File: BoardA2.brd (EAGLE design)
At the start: 44 x 93 mm, 17 parts, among them J1 FEMALE 2x3, T1 2N2222

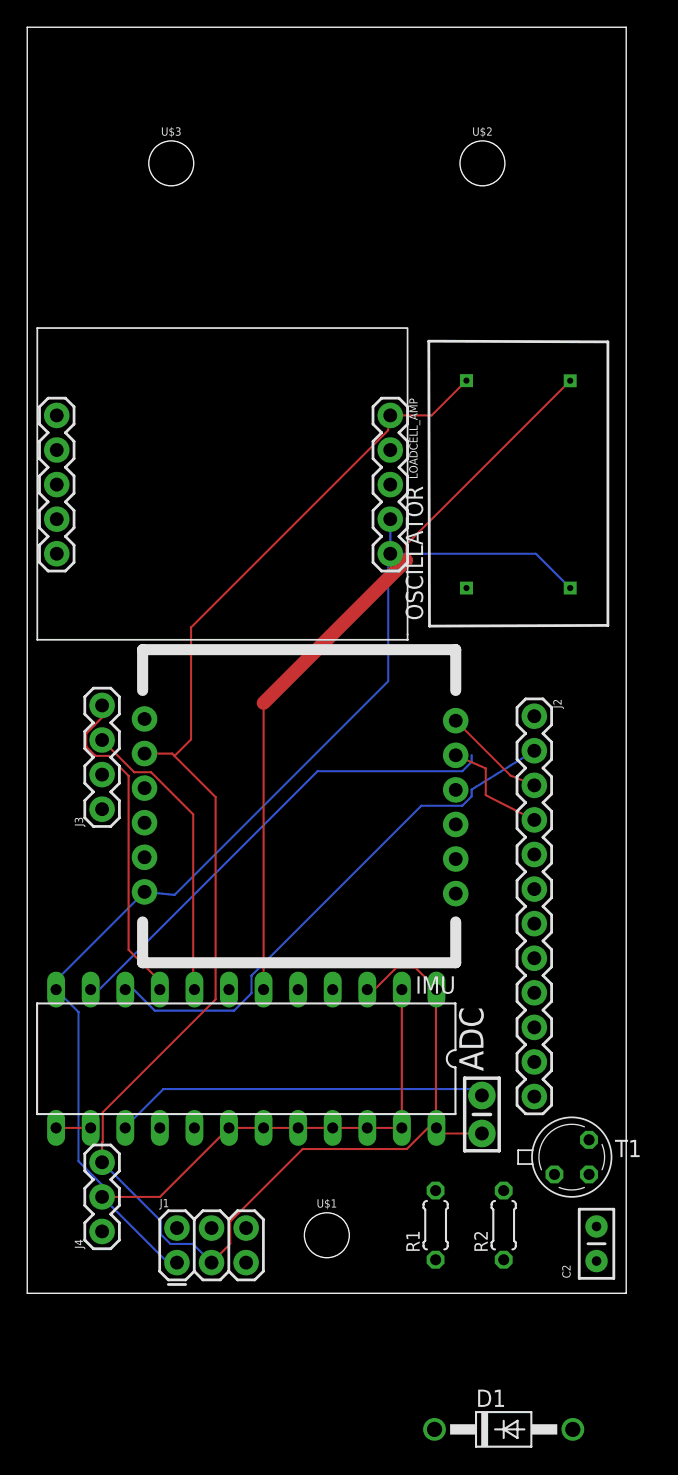
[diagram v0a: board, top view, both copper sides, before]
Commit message: routed middle board
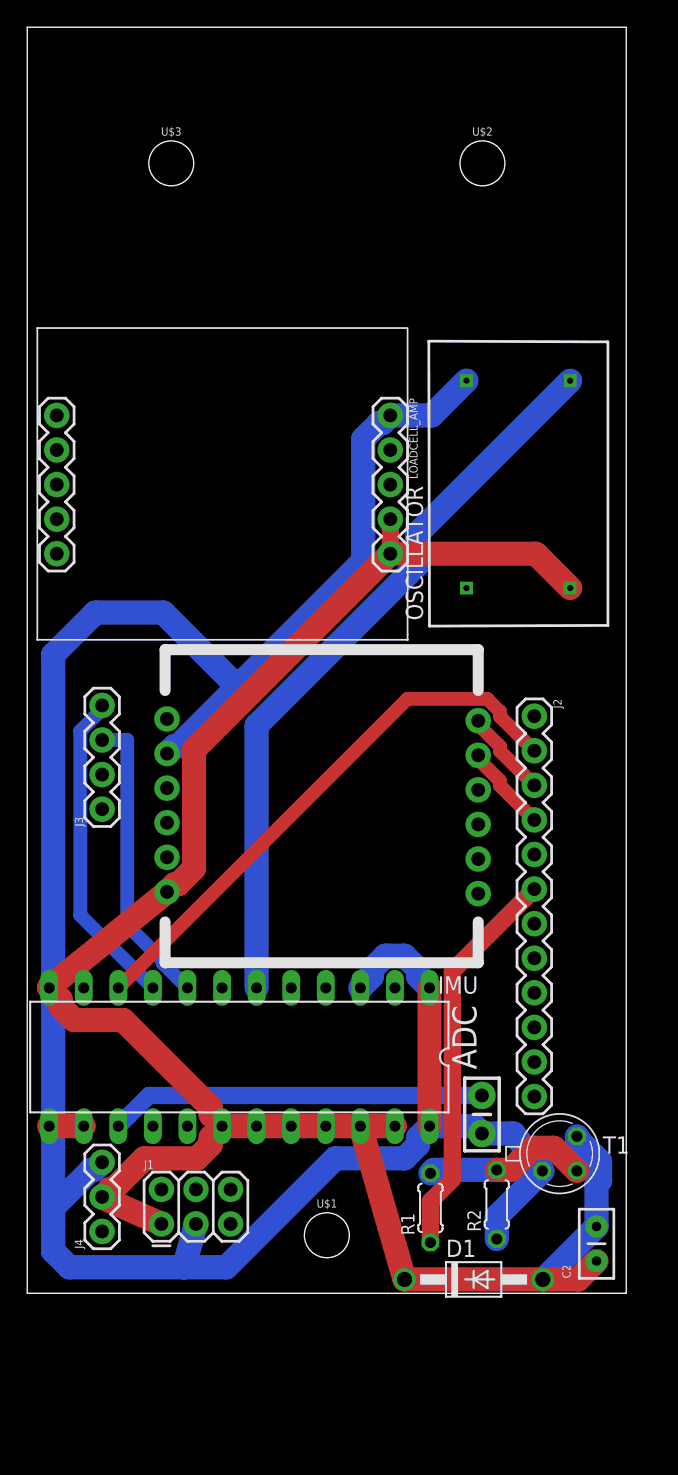
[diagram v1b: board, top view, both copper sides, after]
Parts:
- moved D1 11.2 mm to (32.8, 1.02)
- moved J1 3.06 mm to (9.86, 5.09)
- moved IMU 1.65 mm to (33.1, 24.3)
- moved R2 1.61 mm to (34.5, 6.52)
- moved R1 1.33 mm to (29.6, 6.27)
- moved T1 0.92 mm to (39.1, 10.3)
- moved ADC 0.52 mm to (15.6, 17.4)
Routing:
- net GND: track 128.5 -> 173.9 mm
- net DIN: track 35.4 -> 0.00 mm
- net TEENSY6: track 0.00 -> 29.1 mm
- net 5V: track 118.9 -> 132.1 mm
- net N$6: track 0.00 -> 13.0 mm
- net N$8: track 0.00 -> 12.2 mm
- net TXD: track 8.38 -> 6.46 mm
- net DOUT: track 39.3 -> 41.1 mm
- net RXD: track 7.58 -> 6.46 mm
- net RFS: track 24.2 -> 23.6 mm

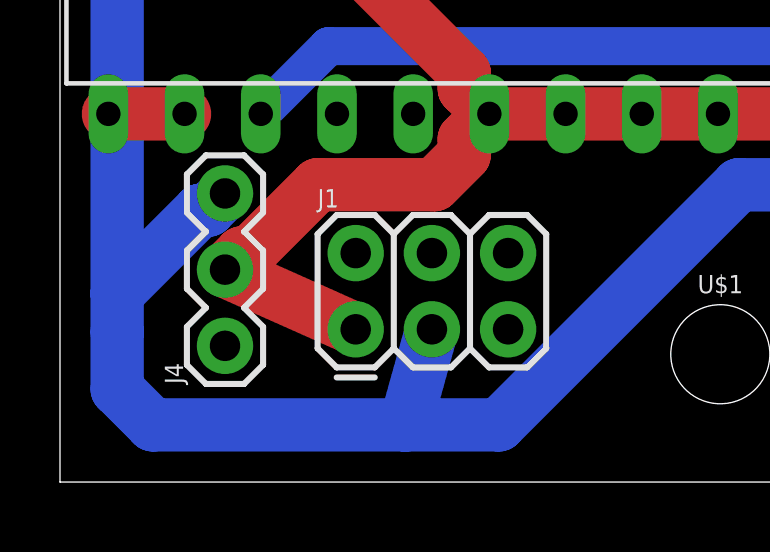
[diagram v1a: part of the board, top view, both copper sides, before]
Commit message: made wire and vias thicker
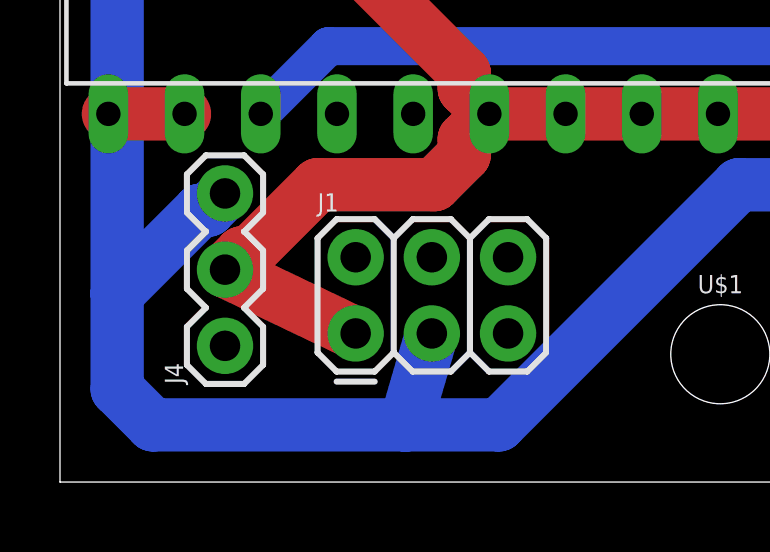
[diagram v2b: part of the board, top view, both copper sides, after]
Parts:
- moved J1 0.14 mm to (9.86, 4.95)
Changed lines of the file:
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@@
 </element>
 <element name="ADC" library="ic-package" library_urn="urn:adsk.eagle:library:239" package="DIL24-4" value="AD7890-10" x="15.582" y="17.353" rot="R180"/>
-<element name="J1" library="SparkFun-Connectors" package="2X3" value="FEMALE 2x3" x="9.857" y="5.091">
-<attribute name="PROD_ID" value="CONN-11566" x="9.857" y="5.091" size="1.778" layer="27" display="off"/>
+<element name="J1" library="SparkFun-Connectors" package="2X3" value="FEMALE 2x3" x="9.8552" y="4.953">
+<attribute name="PROD_ID" value="CONN-11566" x="9.8552" y="4.953" size="1.778" layer="27" display="off"/>
 </element>
 <element name="OSCILLATOR" library="Smartcrutches" package="ECS-100X" value="CLOCK-ECS-100X" x="36.077" y="59.422" rot="R90"/>
@@
 <wire x1="8.59264375" y1="9.9108" x2="6.32064375" y2="7.6388" width="1.778" layer="1"/>
 <wire x1="5.5" y1="7.035" x2="5.5" y2="7.08" width="1.778" layer="1"/>
-<wire x1="9.857" y1="5.091" x2="5.5" y2="7.035" width="1.778" layer="1"/>
+<wire x1="9.8552" y1="4.953" x2="5.5" y2="7.035" width="1.778" layer="1"/>
 <wire x1="3.4470875" y1="20.0708" x2="2.4502" y2="21.0676875" width="1.778" layer="1"/>
 <wire x1="2.4502" y1="21.0676875" x2="2.4502" y2="21.5948" width="1.778" layer="1"/>
@@
 <contactref element="T1" pad="1"/>
 <contactref element="R2" pad="1"/>
-<wire x1="12.397" y1="5.091" x2="11.508" y2="1.905" width="1.778" layer="16"/>
+<wire x1="12.3952" y1="4.953" x2="11.508" y2="1.905" width="1.778" layer="16"/>
 <wire x1="11.508" y1="1.905" x2="3.095" y2="1.905" width="1.778" layer="16"/>
 <wire x1="3.095" y1="1.905" x2="1.905" y2="3.095" width="1.778" layer="16"/>
 <wire x1="4.67935625" y1="9.0612" x2="4.9412" y2="9.0612" width="1.778" layer="16"/>
 <wire x1="4.9412" y1="9.0612" x2="5.5" y2="9.62" width="1.778" layer="16"/>
-<wire x1="1.905" y1="3.095" x2="1.905" y2="5" width="1.778" layer="16"/>
-<wire x1="1.905" y1="5" x2="1.905" y2="6.28684375" width="1.778" layer="16"/>
+<wire x1="1.905" y1="3.095" x2="1.905" y2="6.28684375" width="1.778" layer="16"/>
 <wire x1="1.905" y1="6.28684375" x2="4.67935625" y2="9.0612" width="1.778" layer="16"/>
 <wire x1="27.7169125" y1="9.9108" x2="28.7138" y2="10.9076875" width="1.778" layer="16"/>

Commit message: Teensy Pin Update 1
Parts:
- renumbered J2 to TEENSY1-12
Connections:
- removed net TEENSY9: TEENSY1-12.9
- new net IMU-RX: IMU.7, TEENSY1-12.10
- new net IMU-TX: IMU.8, TEENSY1-12.9
- net DOUT: no longer TEENSY1-12.2
- net RXD: no longer IMU.7
- net TXD: no longer IMU.8
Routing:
- net DOUT: track 41.1 -> 37.6 mm
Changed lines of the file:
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@@
 <element name="IMU" library="Smartcrutches" package="IMU" value="TSS-EM/3Space" x="33.128" y="24.278" rot="R180"/>
 <element name="LOADCELL_AMP" library="Smartcrutches" package="LOADCELLAMP2" value="HX711" x="15.24" y="59.403" rot="R180"/>
-<element name="J2" library="SparkFun-Connectors" package="1X12" value="" x="37.25" y="42.39" rot="R270"/>
+<element name="TEENSY1-12" library="SparkFun-Connectors" package="1X12" value="" x="37.25" y="42.39" rot="R270"/>
 <element name="J3" library="SparkFun-Connectors" package="1X04" value="" x="5.5" y="35.56" rot="R90">
 <attribute name="PROD_ID" value="CONN-09696" x="5.5" y="35.56" size="1.778" layer="27" rot="R90" display="off"/>
@@
 <signal name="DOUT">
 <contactref element="ADC" pad="10"/>
-<contactref element="J2" pad="2"/>
 <wire x1="33.790825" y1="43.6582" x2="34.7282" y2="42.720825" width="1.016" layer="1"/>
 <wire x1="6.692" y1="22.433" x2="6.70370625" y2="22.433" width="1.016" layer="1"/>
 <wire x1="34.7282" y1="42.720825" x2="34.7282" y2="42.3718" width="1.016" layer="1"/>
-<wire x1="34.7282" y1="42.3718" x2="37.25" y2="39.85" width="1.016" layer="1"/>
 <wire x1="6.70370625" y1="22.433" x2="27.92890625" y2="43.6582" width="1.016" layer="1"/>
 <wire x1="27.92890625" y1="43.6582" x2="33.790825" y2="43.6582" width="1.016" layer="1"/>
@@
 </signal>
 <signal name="TXD">
-<contactref element="IMU" pad="8"/>
-<contactref element="J2" pad="4"/>
+<contactref element="TEENSY1-12" pad="4"/>
 <wire x1="34.7282" y1="37.640825" x2="34.7282" y2="37.2918" width="1.016" layer="1"/>
 <wire x1="34.7282" y1="37.2918" x2="37.25" y2="34.77" width="1.016" layer="1"/>
-<wire x1="33.128" y1="39.518" x2="33.128" y2="39.241025" width="1.016" layer="1"/>
 <wire x1="33.128" y1="39.241025" x2="34.7282" y2="37.640825" width="1.016" layer="1"/>
 </signal>
 <signal name="RXD">
-<contactref element="IMU" pad="7"/>
-<contactref element="J2" pad="3"/>
+<contactref element="TEENSY1-12" pad="3"/>
 <wire x1="34.7282" y1="40.180825" x2="34.7282" y2="39.8318" width="1.016" layer="1"/>
 <wire x1="34.7282" y1="39.8318" x2="37.25" y2="37.31" width="1.016" layer="1"/>
-<wire x1="33.128" y1="42.058" x2="33.128" y2="41.781025" width="1.016" layer="1"/>
 <wire x1="33.128" y1="41.781025" x2="34.7282" y2="40.180825" width="1.016" layer="1"/>
 </signal>
@@
 <signal name="TEENSY6">
 <contactref element="R1" pad="1"/>
-<contactref element="J2" pad="6"/>
+<contactref element="TEENSY1-12" pad="6"/>
 <wire x1="29.619" y1="3.73" x2="29.619" y2="6.7625" width="1.27" layer="1"/>
 <wire x1="31.2284" y1="23.6684" x2="37.25" y2="29.69" width="1.27" layer="1"/>
@@
 </signal>
 <signal name="TEENSY1">
-<contactref element="J2" pad="1"/>
-</signal>
-<signal name="TEENSY9">
-<contactref element="J2" pad="9"/>
+<contactref element="TEENSY1-12" pad="1"/>
 </signal>
 <signal name="N$5">
@@
 <contactref element="LOADCELL_AMP" pad="2"/>
 </signal>
+<signal name="IMU-RX">
+<contactref element="IMU" pad="7"/>
+<contactref element="TEENSY1-12" pad="10"/>
+<wire x1="37.25" y1="19.53" x2="33.128" y2="42.058" width="0" layer="19" extent="1-1"/>
+</signal>
+<signal name="IMU-TX">
+<contactref element="TEENSY1-12" pad="9"/>
+<contactref element="IMU" pad="8"/>
+<wire x1="37.25" y1="22.07" x2="33.128" y2="39.518" width="0" layer="19" extent="1-1"/>
+</signal>
 </signals>

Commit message: Teensy Pin Update2
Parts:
- removed J3: (no value), SparkFun-Connectors:1X04
- added LOWERLOADCELL: (no value), SparkFun-Connectors:1X05
- added MOTOR: (no value), SparkFun-Connectors:1X02
- renumbered J4 to TEENSYU
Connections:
- net CONVST renamed ADC-CONVST
- net SCLK renamed ADC-SCLK
- net TEENSY6 renamed MOTOR
- removed net DIN: ADC.11
- removed net DOUT: ADC.10
- removed net N$2: ADC.17
- removed net N$5: LOADCELL_AMP.3
- removed net N$7: LOADCELL_AMP.2
- removed net RFS: ADC.9, J3.4
- removed net RXD: TEENSY1-12.3
- removed net SLCK: J3.1
- removed net TFS: ADC.8, J3.3
- removed net TXD: TEENSY1-12.4
- removed net UPPER1: ADC.16
- new net ADC-CH1: ADC.16, J1.2
- new net ADC-CH2: ADC.17, J1.4
- new net ADC-DIN: ADC.11, TEENSY1-12.11
- new net ADC-DOUT: ADC.10, TEENSY1-12.12
- new net ADC-RFS: ADC.9, TEENSY1-12.8
- new net ADC-SLK: TEENSY1-12.5
- new net ADC-TFS: ADC.8, TEENSY1-12.7
- new net AMP-CLK: LOADCELL_AMP.2, TEENSY1-12.4
- new net AMP-DAT: LOADCELL_AMP.3, TEENSY1-12.3
- net 5V: now also TEENSYU.1; no longer TEENSYU.2
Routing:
- net DOUT: track 37.6 -> 0.00 mm
- net ADC-DOUT: track 0.00 -> 37.6 mm
- net RFS: track 23.6 -> 0.00 mm
- net ADC-RFS: track 0.00 -> 23.3 mm
- net TFS: track 21.9 -> 0.00 mm
- net ADC-TFS: track 0.00 -> 20.0 mm
- net TXD: track 6.18 -> 0.00 mm
- net RXD: track 6.18 -> 0.00 mm
- net AMP-CLK: track 0.00 -> 6.18 mm
- net 5V: track 132.1 -> 131.3 mm
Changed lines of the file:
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@@
 <element name="LOADCELL_AMP" library="Smartcrutches" package="LOADCELLAMP2" value="HX711" x="15.24" y="59.403" rot="R180"/>
 <element name="TEENSY1-12" library="SparkFun-Connectors" package="1X12" value="" x="37.25" y="42.39" rot="R270"/>
-<element name="J3" library="SparkFun-Connectors" package="1X04" value="" x="5.5" y="35.56" rot="R90">
-<attribute name="PROD_ID" value="CONN-09696" x="5.5" y="35.56" size="1.778" layer="27" rot="R90" display="off"/>
-</element>
 <element name="U$1" library="SparkFun-Hardware" package="STAND-OFF" value="" x="22.01" y="4.26"/>
 <element name="U$2" library="SparkFun-Hardware" package="STAND-OFF" value="" x="33.44" y="83"/>
 <element name="U$3" library="SparkFun-Hardware" package="STAND-OFF" value="" x="10.58" y="83"/>
-<element name="J4" library="SparkFun-Connectors" package="1X03" value="" x="5.5" y="4.54" rot="R90"/>
+<element name="TEENSYU" library="SparkFun-Connectors" package="1X03" value="" x="5.5" y="4.54" rot="R90"/>
 <element name="R1" library="resistor" library_urn="urn:adsk.eagle:library:348" package="0204/5" value="1kohm" x="29.619" y="6.27" rot="R90"/>
 <element name="R2" library="resistor" library_urn="urn:adsk.eagle:library:348" package="0204/5" value="10kohm" x="34.492" y="6.524" rot="R90"/>
@@
 <element name="D1" library="diode" library_urn="urn:adsk.eagle:library:210" package="DO41-10" value="1N4004" x="32.794" y="1.016"/>
 <element name="C2" library="SparkFun-Passives" package="CAP-PTH-SMALL2" value="0.1uf" x="41.82" y="2.366" rot="R90"/>
+<element name="MOTOR" library="SparkFun-Connectors" package="1X02" value="" x="41.364" y="22.507" rot="R90"/>
+<element name="LOWERLOADCELL" library="SparkFun-Connectors" package="1X05" value="" x="12.239" y="91.002" rot="R180"/>
 </elements>
 <signals>
@@
 <contactref element="LOADCELL_AMP" pad="5"/>
 <contactref element="LOADCELL_AMP" pad="4"/>
-<contactref element="J4" pad="2"/>
 <contactref element="D1" pad="C"/>
 <contactref element="C2" pad="1"/>
@@
 <wire x1="13.4738" y1="10.9076875" x2="12.4769125" y2="9.9108" width="1.778" layer="1"/>
 <wire x1="6.0588" y1="7.6388" x2="6.32064375" y2="7.6388" width="1.778" layer="1"/>
-<wire x1="5.5" y1="7.08" x2="6.0588" y2="7.6388" width="1.778" layer="1"/>
 <wire x1="14.312" y1="12.273" x2="13.4738" y2="11.4348" width="1.778" layer="1"/>
 <wire x1="13.4738" y1="11.4348" x2="13.4738" y2="10.9076875" width="1.778" layer="1"/>
 <wire x1="12.4769125" y1="9.9108" x2="8.59264375" y2="9.9108" width="1.778" layer="1"/>
 <wire x1="8.59264375" y1="9.9108" x2="6.32064375" y2="7.6388" width="1.778" layer="1"/>
-<wire x1="5.5" y1="7.035" x2="5.5" y2="7.08" width="1.778" layer="1"/>
 <wire x1="9.8552" y1="4.953" x2="5.5" y2="7.035" width="1.778" layer="1"/>
 <wire x1="3.4470875" y1="20.0708" x2="2.4502" y2="21.0676875" width="1.778" layer="1"/>
@@
 <wire x1="37.366" y1="54.323" x2="39.887" y2="51.802" width="1.778" layer="1"/>
 <wire x1="26.67" y1="54.323" x2="26.67" y2="56.863" width="1.27" layer="1"/>
+<contactref element="TEENSYU" pad="1"/>
 <wire x1="27.012" y1="12.273" x2="27.012" y2="22.433" width="0" layer="19" extent="1-1"/>
 <wire x1="1.612" y1="22.433" x2="1.905" y2="22.14" width="0" layer="19" extent="1-1"/>
+<wire x1="5.5" y1="7.035" x2="6.0588" y2="7.6388" width="0" layer="19" extent="1-1"/>
+<wire x1="5.5" y1="4.54" x2="5.5" y2="7.035" width="0" layer="19" extent="1-1"/>
 </signal>
 <signal name="N$1">
@@
 <contactref element="LOADCELL_AMP" pad="1"/>
 <contactref element="OSCILLATOR" pad="7"/>
-<contactref element="J4" pad="3"/>
+<contactref element="TEENSYU" pad="3"/>
 <contactref element="T1" pad="1"/>
 <contactref element="R2" pad="1"/>
@@
 <wire x1="16.852" y1="41.70315625" x2="28.6512" y2="53.50235625" width="1.778" layer="16"/>
 </signal>
-<signal name="UPPER1">
-<contactref element="ADC" pad="16"/>
-</signal>
-<signal name="N$2">
-<contactref element="ADC" pad="17"/>
-</signal>
-<signal name="DIN">
+<signal name="ADC-DIN">
 <contactref element="ADC" pad="11"/>
-</signal>
-<signal name="DOUT">
+<contactref element="TEENSY1-12" pad="11"/>
+<wire x1="4.152" y1="22.433" x2="37.25" y2="16.99" width="0" layer="19" extent="1-1"/>
+</signal>
+<signal name="ADC-DOUT">
 <contactref element="ADC" pad="10"/>
 <wire x1="33.790825" y1="43.6582" x2="34.7282" y2="42.720825" width="1.016" layer="1"/>
@@
 <wire x1="6.70370625" y1="22.433" x2="27.92890625" y2="43.6582" width="1.016" layer="1"/>
 <wire x1="27.92890625" y1="43.6582" x2="33.790825" y2="43.6582" width="1.016" layer="1"/>
-</signal>
-<signal name="RFS">
+<contactref element="TEENSY1-12" pad="12"/>
+<wire x1="34.7282" y1="42.3718" x2="37.25" y2="14.45" width="0" layer="19" extent="1-1"/>
+</signal>
+<signal name="ADC-RFS">
 <contactref element="ADC" pad="9"/>
-<contactref element="J3" pad="4"/>
-<wire x1="5.5" y1="43.18" x2="5.5" y2="42.903025" width="1.016" layer="16"/>
 <wire x1="5.5" y1="42.903025" x2="3.8998" y2="41.302825" width="1.016" layer="16"/>
 <wire x1="3.8998" y1="41.302825" x2="3.8998" y2="27.7652" width="1.016" layer="16"/>
 <wire x1="3.8998" y1="27.7652" x2="9.232" y2="22.433" width="1.016" layer="16"/>
-</signal>
-<signal name="TFS">
+<contactref element="TEENSY1-12" pad="8"/>
+<wire x1="9.232" y1="22.433" x2="37.25" y2="24.61" width="0" layer="19" extent="1-1"/>
+</signal>
+<signal name="ADC-TFS">
 <contactref element="ADC" pad="8"/>
-<contactref element="J3" pad="3"/>
-<wire x1="5.5" y1="40.64" x2="7.348975" y2="40.64" width="1.016" layer="16"/>
 <wire x1="7.348975" y1="40.64" x2="7.348975" y2="27.034325" width="1.016" layer="16"/>
 <wire x1="9.9432" y1="24.4401" x2="9.9432" y2="24.2618" width="1.016" layer="16"/>
 <wire x1="9.9432" y1="24.2618" x2="11.772" y2="22.433" width="1.016" layer="16"/>
 <wire x1="7.348975" y1="27.034325" x2="9.9432" y2="24.4401" width="1.016" layer="16"/>
-</signal>
-<signal name="SCLK">
+<contactref element="TEENSY1-12" pad="7"/>
+<wire x1="11.772" y1="22.433" x2="37.25" y2="27.15" width="0" layer="19" extent="1-1"/>
+</signal>
+<signal name="ADC-SCLK">
 <contactref element="ADC" pad="7"/>
 </signal>
-<signal name="CONVST">
+<signal name="ADC-CONVST">
 <contactref element="ADC" pad="5"/>
 </signal>
 <signal name="N$11">
 <contactref element="ADC" pad="4"/>
-</signal>
-<signal name="TXD">
-<contactref element="TEENSY1-12" pad="4"/>
-<wire x1="34.7282" y1="37.640825" x2="34.7282" y2="37.2918" width="1.016" layer="1"/>
-<wire x1="34.7282" y1="37.2918" x2="37.25" y2="34.77" width="1.016" layer="1"/>
-<wire x1="33.128" y1="39.241025" x2="34.7282" y2="37.640825" width="1.016" layer="1"/>
-</signal>
-<signal name="RXD">
-<contactref element="TEENSY1-12" pad="3"/>
-<wire x1="34.7282" y1="40.180825" x2="34.7282" y2="39.8318" width="1.016" layer="1"/>
-<wire x1="34.7282" y1="39.8318" x2="37.25" y2="37.31" width="1.016" layer="1"/>
-<wire x1="33.128" y1="41.781025" x2="34.7282" y2="40.180825" width="1.016" layer="1"/>
-</signal>
-<signal name="SLCK">
-<contactref element="J3" pad="1"/>
 </signal>
 <signal name="N$6">
@@
 <wire x1="38.6792" y1="10.6858" x2="40.381" y2="8.984" width="1.778" layer="1"/>
 </signal>
-<signal name="TEENSY6">
+<signal name="MOTOR">
 <contactref element="R1" pad="1"/>
 <contactref element="TEENSY1-12" pad="6"/>
@@
 <contactref element="TEENSY1-12" pad="1"/>
 </signal>
-<signal name="N$5">
+<signal name="AMP-DAT">
 <contactref element="LOADCELL_AMP" pad="3"/>
-</signal>
-<signal name="N$7">
+<contactref element="TEENSY1-12" pad="3"/>
+<wire x1="37.25" y1="37.31" x2="26.67" y2="59.403" width="0" layer="19" extent="1-1"/>
+</signal>
+<signal name="AMP-CLK">
 <contactref element="LOADCELL_AMP" pad="2"/>
+<contactref element="TEENSY1-12" pad="4"/>
+<wire x1="34.7282" y1="37.640825" x2="34.7282" y2="37.2918" width="1.016" layer="1"/>
+<wire x1="34.7282" y1="37.2918" x2="37.25" y2="34.77" width="1.016" layer="1"/>
+<wire x1="33.128" y1="39.241025" x2="34.7282" y2="37.640825" width="1.016" layer="1"/>
+<wire x1="33.128" y1="39.241025" x2="26.67" y2="61.943" width="0" layer="19" extent="1-1"/>
 </signal>
 <signal name="IMU-RX">
@@
 <wire x1="37.25" y1="22.07" x2="33.128" y2="39.518" width="0" layer="19" extent="1-1"/>
 </signal>
+<signal name="ADC-SLK">
+<contactref element="TEENSY1-12" pad="5"/>
+</signal>
+<signal name="ADC-CH1">
+<contactref element="ADC" pad="16"/>
+<contactref element="J1" pad="2"/>
+<wire x1="9.8552" y1="7.493" x2="9.232" y2="12.273" width="0" layer="19" extent="1-1"/>
+</signal>
+<signal name="ADC-CH2">
+<contactref element="ADC" pad="17"/>
+<contactref element="J1" pad="4"/>
+<wire x1="12.3952" y1="7.493" x2="11.772" y2="12.273" width="0" layer="19" extent="1-1"/>
+</signal>
 </signals>
